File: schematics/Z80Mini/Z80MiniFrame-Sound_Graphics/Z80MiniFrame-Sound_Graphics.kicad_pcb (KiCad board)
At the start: 2 copper layers, 194.3 x 105.4 mm, 65 parts, among them J1 Conn_02x20_Odd_Even, J2 RGB Out, U1 TMS9929A, U12 74LS32, U13 74LS139, U14 TL084, U2 74LS574, U3 74LS574, U4 74LS574, U5 AS6C62256-55PCN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

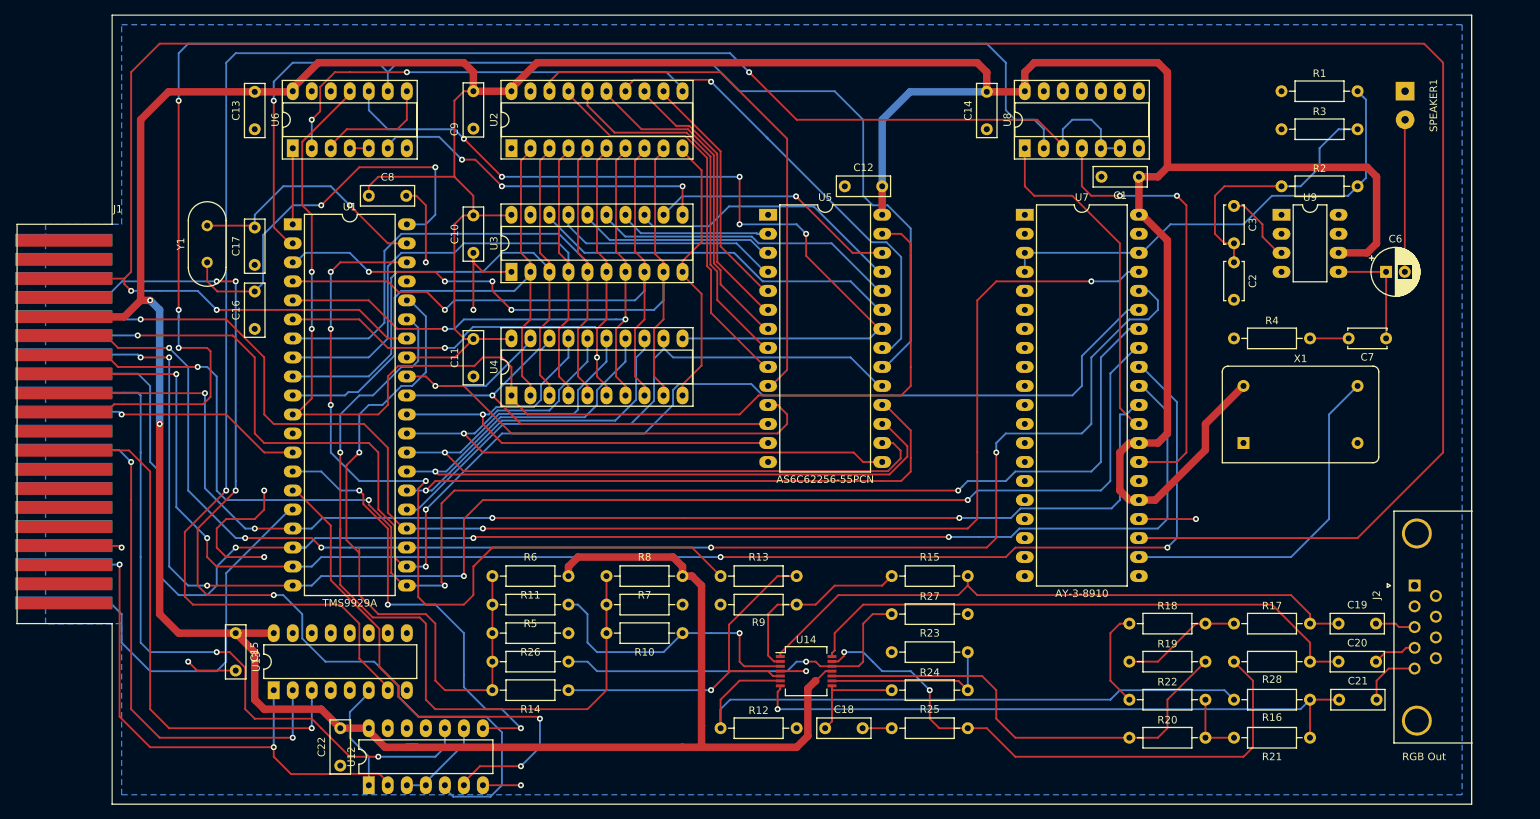
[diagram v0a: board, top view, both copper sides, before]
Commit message: Latest graphics and sound card schematic and PCB modifications
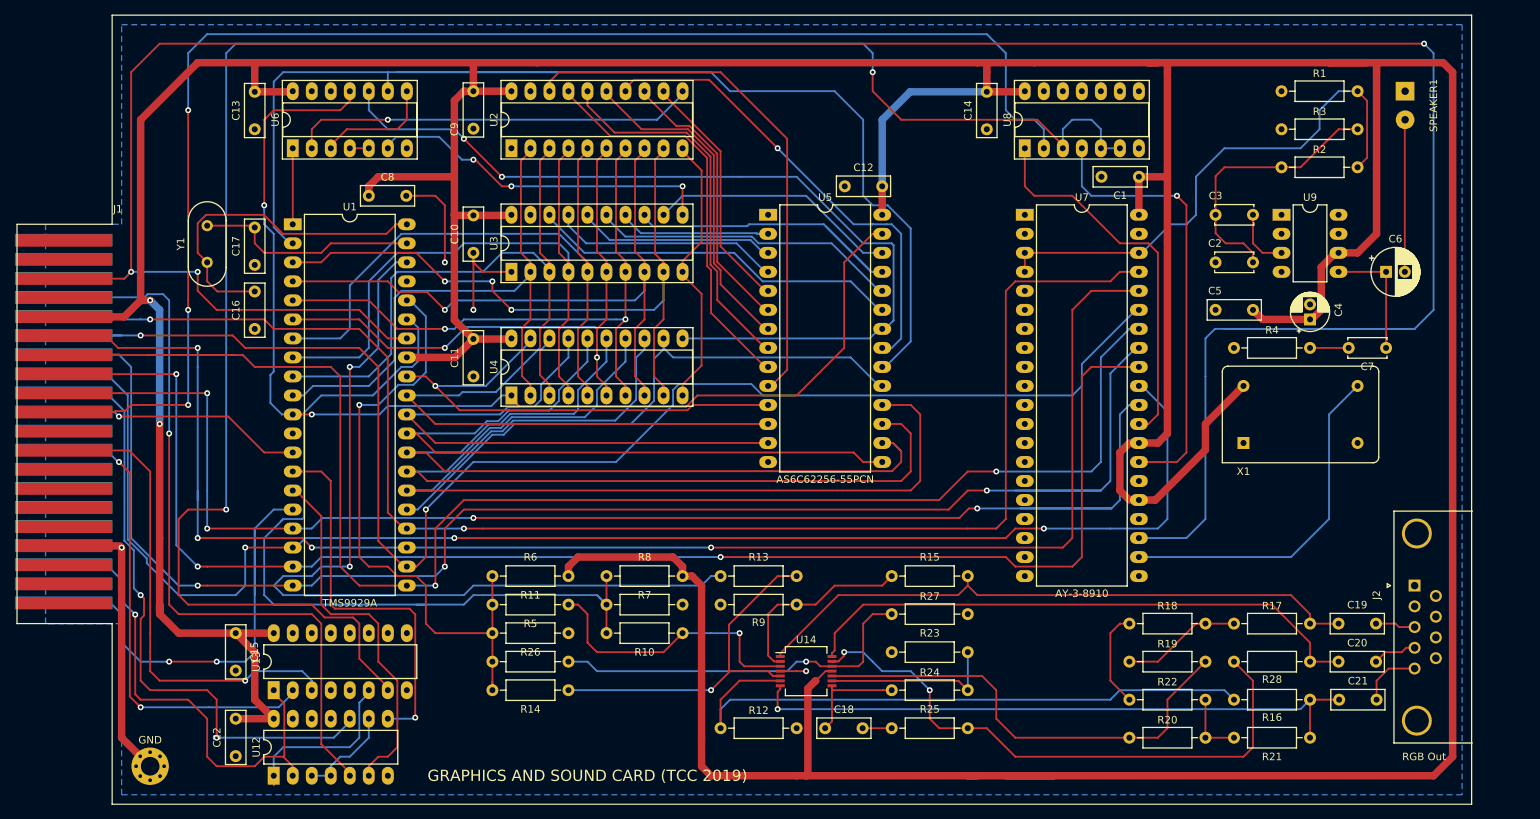
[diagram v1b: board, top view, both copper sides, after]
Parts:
- added C4: 10uF, Capacitor_THT:CP_Radial_D5.0mm_P2.00mm, F.Cu at (218.4, 82.5)
- added C5: 0.1uF, Capacitor_THT:C_Disc_D7.0mm_W2.5mm_P5.00mm, F.Cu at (210.8, 81.3)
- added GND: MountingHole_2.5mm_Pad_Via, MountingHole:MountingHole_2.5mm_Pad_Via, F.Cu at (63.5, 142.2)
- moved C22 14.0 mm to (74.9, 140.9)
- moved U12 12.8 mm to (80.0, 143.5)
- moved C3 2.80 mm to (210.8, 68.6), turned to 180 degrees
- moved R2 2.54 mm to (214.6, 62.2)
- moved C2 2.54 mm to (210.8, 74.9), turned to 180 degrees
- moved C7 1.27 mm to (228.6, 86.4)
- moved R4 1.27 mm to (208.3, 86.4)
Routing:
- net VCC: track 627.4 -> 839.1 mm, vias 2 -> 3
- net Net-(U1-Pad2): track 148.0 -> 188.3 mm, vias 1 -> 0
- net /graphicsProcessor/RD: track 134.3 -> 104.2 mm, vias 4 -> 1
- net /graphicsProcessor/RESET: track 352.9 -> 380.0 mm, vias 2 -> 3
- net Net-(U1-Pad15): track 70.0 -> 49.4 mm, vias 2 -> 0
- net /graphicsProcessor/WR: track 102.4 -> 81.8 mm
- net /D3: track 198.7 -> 215.2 mm, vias 4 -> 2
- net /D7: track 172.1 -> 187.5 mm
- net /A5: track 77.9 -> 63.5 mm
- net /graphicsProcessor/IORQ: track 76.0 -> 64.5 mm, vias 2 -> 1
- net /graphicsProcessor/VD1: track 60.8 -> 72.3 mm, vias 1 -> 0
- net Net-(U1-Pad11): track 166.1 -> 154.9 mm
- net /graphicsProcessor/INT: track 58.2 -> 69.2 mm, vias 0 -> 2
- net Net-(U1-Pad14): track 61.1 -> 51.4 mm, vias 3 -> 1
- net Net-(C16-Pad2): track 54.9 -> 45.3 mm, vias 2 -> 0
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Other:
- net class GND added: clearance 0.2, trace_width 1, via_dia 0.8, via_drill 0.4
- board text added: "GRAPHICS AND SOUND CARD (TCC 2019)"

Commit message: Latest modifications on Graphics-Sound card
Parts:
- added J3: Conn_01x03_Male, Connector_PinHeader_2.00mm:PinHeader_1x03_P2.00mm_Vertical, F.Cu at (208.3, 59.7)
- added JP1: PREAMP_MONO, Connector_PinHeader_2.00mm:PinHeader_2x03_P2.00mm_Vertical, F.Cu at (208.3, 50.8)
- moved R2 10.2 mm to (224.8, 62.2), turned to 180 degrees
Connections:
- R1 pad 2: Net-(R1-Pad2) -> Net-(JP1-Pad1)
- R2 pad 2: Net-(R1-Pad2) -> Net-(JP1-Pad1)
- U7 pad 3: Net-(R1-Pad2) -> Net-(J3-Pad2)
- U7 pad 38: Net-(R1-Pad2) -> Net-(J3-Pad1)
- U7 pad 4: Net-(R1-Pad2) -> Net-(J3-Pad3)
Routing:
- net Net-(R1-Pad2): track 71.6 -> 0.00 mm
- net Net-(J3-Pad3): track 0.00 -> 52.3 mm
- net Net-(J3-Pad2): track 0.00 -> 40.6 mm
- net Net-(JP1-Pad1): track 0.00 -> 34.4 mm
- net Net-(J3-Pad1): track 0.00 -> 26.4 mm
- net Net-(U7-Pad22): track 46.9 -> 40.9 mm
- net Net-(U7-Pad29): track 51.6 -> 48.3 mm
- net /soundGeneration/SND_SEL: track 249.6 -> 251.4 mm

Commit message: Latest modifications
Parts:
- added J4: IO_PORT, Connector_IDC:IDC-Header_2x08_P2.54mm_Vertical, F.Cu at (229.9, 102.9)
- moved R4 16.9 mm to (224.8, 82.5)
- moved C3 14.5 mm to (224.8, 64.8)
- moved C7 14.2 mm to (234.9, 73.7), turned to 270 degrees
- moved C2 12.0 mm to (217.2, 64.8)
- moved C4 10.2 mm to (209.6, 77.5), turned to 270 degrees
- moved C5 7.73 mm to (209.6, 73.7), turned to 90 degrees
- moved J2 3.81 mm to (232.4, 121.9)
- moved X1 3.81 mm to (209.6, 95.2)
- moved R2 2.54 mm to (224.8, 59.7)
- moved R1 1.27 mm to (214.6, 50.8)
- moved R3 1.27 mm to (214.6, 55.9)
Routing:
- net Net-(J4-Pad16): track 0.00 -> 71.2 mm, vias 0 -> 1
- net Net-(J4-Pad3): track 0.00 -> 60.8 mm, vias 0 -> 1
- net Net-(J4-Pad15): track 0.00 -> 55.4 mm, vias 0 -> 1
- net Net-(J4-Pad5): track 0.00 -> 54.0 mm
- net Net-(J4-Pad1): track 0.00 -> 48.8 mm
- net Net-(J4-Pad7): track 0.00 -> 48.6 mm
- net Net-(J4-Pad9): track 0.00 -> 43.5 mm
- net Net-(J4-Pad11): track 0.00 -> 41.6 mm
- net Net-(J4-Pad13): track 0.00 -> 39.3 mm
- net /graphicsProcessor/RESET: track 380.0 -> 348.7 mm, vias 3 -> 4
- net Net-(U7-Pad22): track 40.9 -> 71.7 mm
- net Net-(C2-Pad1): track 36.5 -> 15.0 mm
- net /D7: track 187.5 -> 172.2 mm
- net /D6: track 198.1 -> 213.4 mm, vias 3 -> 4
- net /D4: track 205.8 -> 192.3 mm
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
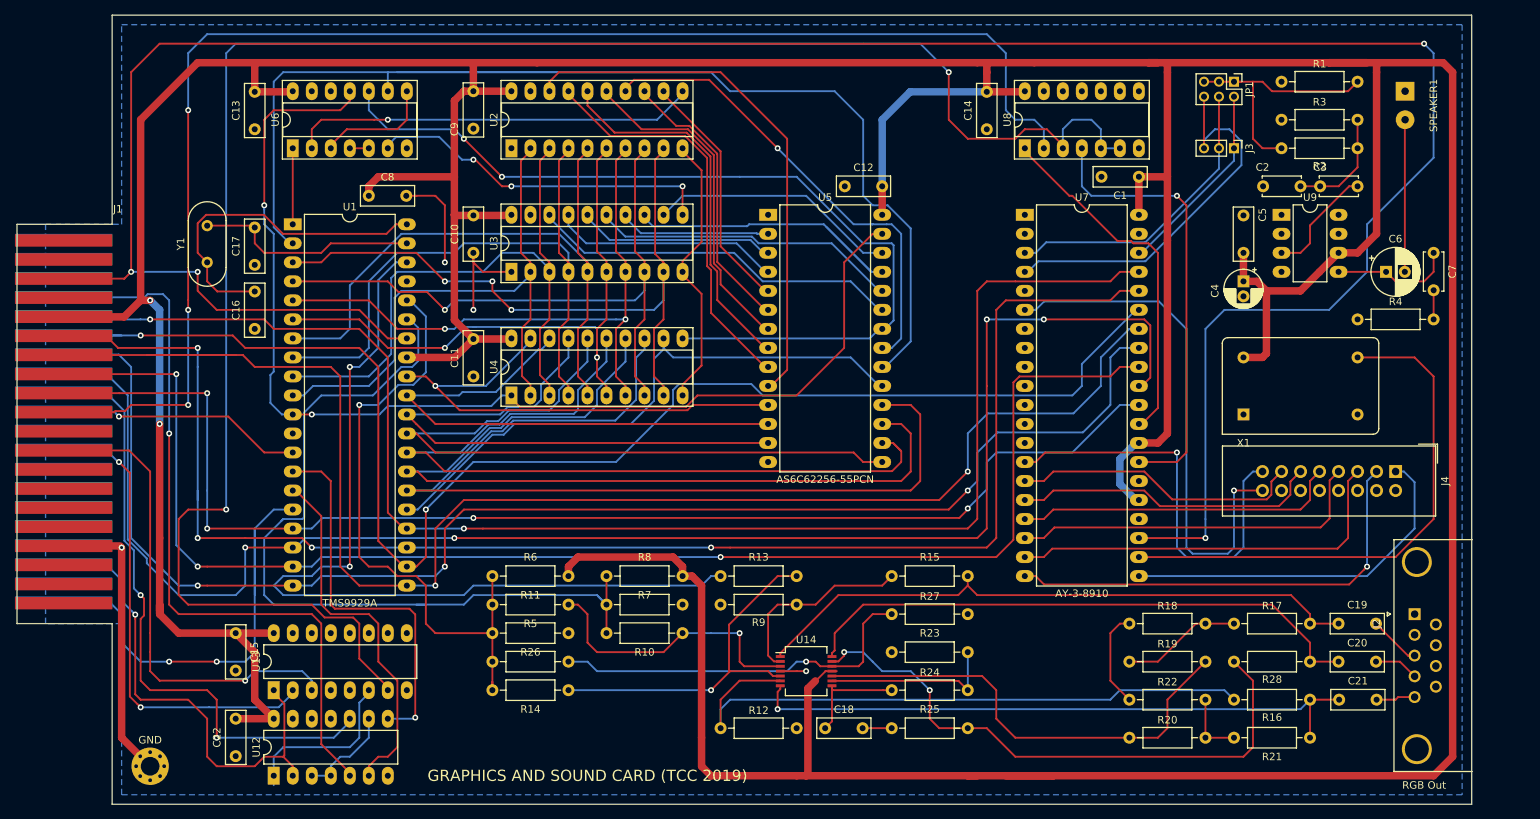
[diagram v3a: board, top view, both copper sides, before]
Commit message: Latest modifications and update to v1.1 and first successifully VDP routines test.
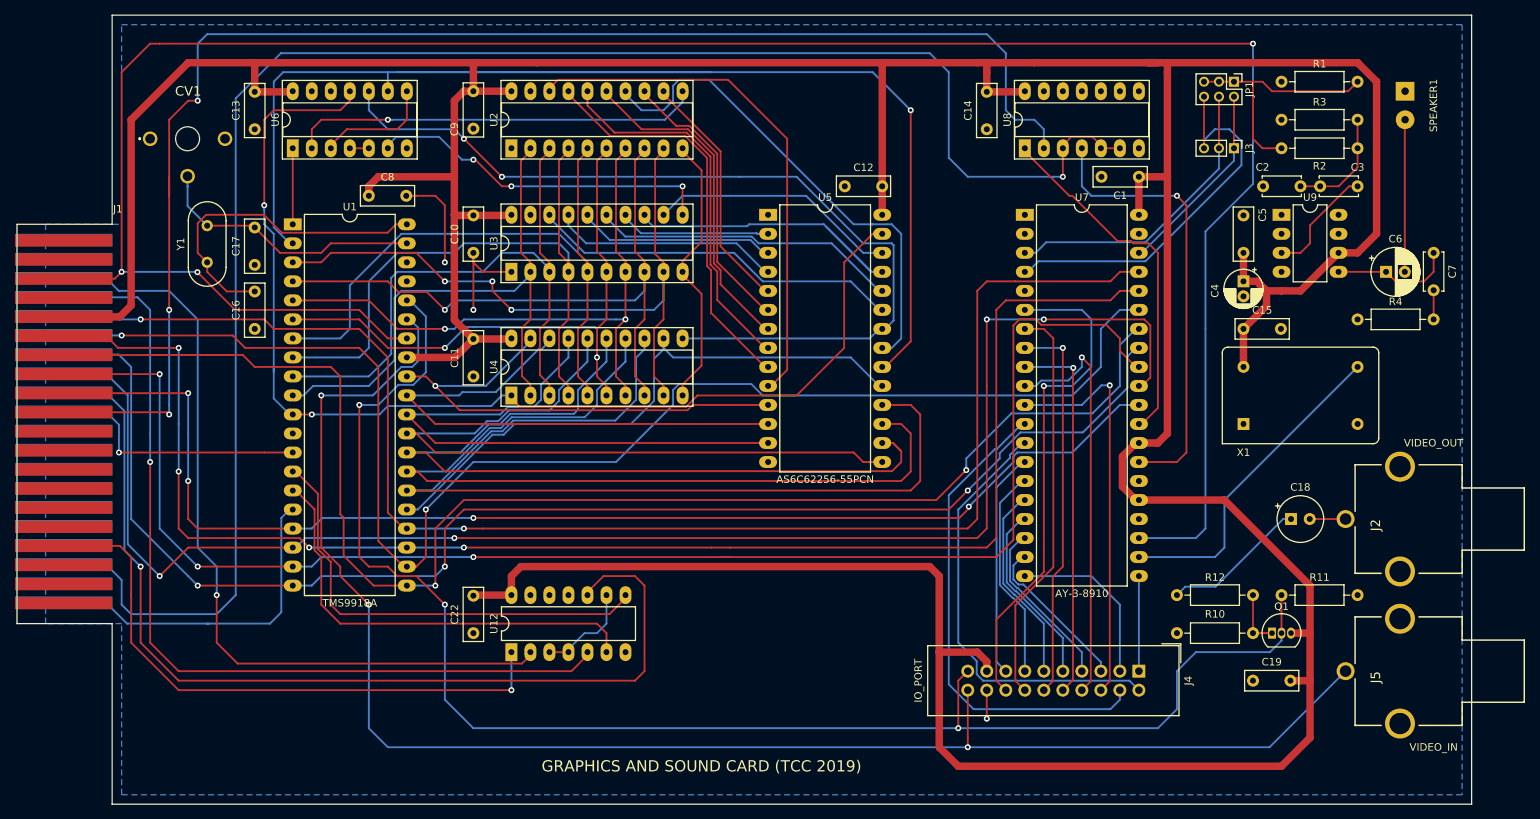
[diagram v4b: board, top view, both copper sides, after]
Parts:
- removed C20, C21: 47pF, Capacitor_THT:C_Disc_D7.0mm_W2.5mm_P5.00mm
- removed GND: MountingHole_2.5mm_Pad_Via, MountingHole:MountingHole_2.5mm_Pad_Via
- removed R13, R14, R15, R16, R17, R19, R20, R21, R23, R24, R25, R26, R9: 100K, Resistor_THT:R_Axial_DIN0207_L6.3mm_D2.5mm_P10.16mm_Horizontal
- removed R18: 47K, Resistor_THT:R_Axial_DIN0207_L6.3mm_D2.5mm_P10.16mm_Horizontal
- removed R22: 12K, Resistor_THT:R_Axial_DIN0207_L6.3mm_D2.5mm_P10.16mm_Horizontal
- removed R27, R28: 170K, Resistor_THT:R_Axial_DIN0207_L6.3mm_D2.5mm_P10.16mm_Horizontal
- removed R5, R7: 1K, Resistor_THT:R_Axial_DIN0207_L6.3mm_D2.5mm_P10.16mm_Horizontal
- removed R6, R8: 2K, Resistor_THT:R_Axial_DIN0207_L6.3mm_D2.5mm_P10.16mm_Horizontal
- removed U13: 74LS139, Package_DIP:DIP-16_W7.62mm_LongPads
- removed U14: TL084, Package_SO:SSOP-14_5.3x6.2mm_P0.65mm
- added CV1: 5-50pF, Capacitor_THT:BFC280831659, F.Cu at (63.5, 58.4)
- added J5: COMP_VIDEOIN, Connector:RCA_Female_902, F.Cu at (238.8, 129.5)
- added Q1: 2N3904, Package_TO_SOT_THT:TO-92_Inline, F.Cu at (213.4, 124.5)
- C16: value 100nF -> 33pf
- C17: value 100nF -> 33pF
- C18: value 47pF -> 220uF; footprint Capacitor_THT:C_Disc_D7.0mm_W2.5mm_P5.00mm -> Capacitor_THT:CP_Radial_Tantal_D6.0mm_P2.50mm
- C19: value 47pF -> 100nF
- J2: value RGB Out -> COMP_VIDEOUT; footprint Connector_Dsub:DSUB-9_Female_Horizontal_P2.77x2.84mm_EdgePinOffset4.94mm_Housed_MountingHolesOffset7.48mm -> Connector:RCA_Female_902
- J4: footprint Connector_IDC:IDC-Header_2x08_P2.54mm_Vertical -> Connector_IDC:IDC-Header_2x10_P2.54mm_Vertical
- R10, R12: value 100K -> 75R
- R11: value 100K -> 470R
- U1: value TMS9929A -> TMS9918A
- Y1: value Crystal -> 10.73MHz
- moved C15 140.6 mm to (209.6, 83.8), turned to 0 degrees
- moved R11 95.3 mm to (214.6, 119.4), turned to 0 degrees
- moved R10 76.2 mm to (210.8, 124.5)
- moved C18 68.2 mm to (215.9, 109.2)
- moved R12 63.5 mm to (200.7, 119.4)
- moved J4 43.4 mm to (195.6, 129.5)
- moved U12 35.8 mm to (111.8, 127.0)
- moved C22 35.7 mm to (106.7, 124.5)
- moved J2 14.2 mm to (238.8, 109.2)
- moved C19 13.7 mm to (210.8, 130.8)
- moved X1 1.27 mm to (209.6, 96.5)
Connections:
- C19 pad 1: /graphicsProcessor/RYBYRGBConverter/RED -> GND
- C19 pad 2: /graphicsProcessor/RYBYRGBConverter/R -> VCC
- J1 pad 23: /A4 -> Net-(J1-Pad23)
- J1 pad 24: /A5 -> Net-(J1-Pad24)
- J1 pad 33: GND -> /graphicsProcessor/VD_SEL
- J1 pad 36: /graphicsProcessor/IORQ -> /soundGeneration/SND_SEL
- J1 pad 6: Net-(J1-Pad6) -> /graphicsProcessor/IORQ
- J2 pad 1: GND -> Net-(C18-Pad2)
- J2 pad 3: /graphicsProcessor/RYBYRGBConverter/R -> (no net)
- R10 pad 1: Net-(R10-Pad1) -> Net-(Q1-Pad1)
- R10 pad 2: /graphicsProcessor/RYBYRGBConverter/R-Y -> GND
- R11 pad 1: Net-(R10-Pad1) -> /graphicsProcessor/COMVID
- R11 pad 2: /graphicsProcessor/RYBYRGBConverter/Y -> GND
- R12 pad 1: Net-(R12-Pad1) -> Net-(C18-Pad1)
- R12 pad 2: GND -> Net-(Q1-Pad1)
- U1 pad 35: /graphicsProcessor/RYBYRGBConverter/R-Y -> /graphicsProcessor/EXTV
- U1 pad 36: /graphicsProcessor/RYBYRGBConverter/Y -> /graphicsProcessor/COMVID
- U1 pad 38: /graphicsProcessor/RYBYRGBConverter/B-Y -> Net-(U1-Pad38)
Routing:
- net /graphicsProcessor/EXTV: track 0.00 -> 211.7 mm, vias 0 -> 3
- net /graphicsProcessor/COMVID: track 0.00 -> 204.1 mm, vias 0 -> 3
- net VCC: track 828.6 -> 662.2 mm, vias 2 -> 0
- net /graphicsProcessor/RYBYRGBConverter/B-Y: track 117.9 -> 0.00 mm, vias 2 -> 0
- net /graphicsProcessor/RYBYRGBConverter/R-Y: track 110.7 -> 0.00 mm
- net Net-(R12-Pad1): track 85.6 -> 0.00 mm
- net /graphicsProcessor/RYBYRGBConverter/BLUE: track 83.9 -> 0.00 mm, vias 1 -> 0
- net /graphicsProcessor/RYBYRGBConverter/Y: track 83.2 -> 0.00 mm, vias 1 -> 0
- net /graphicsProcessor/RYBYRGBConverter/RED: track 82.9 -> 0.00 mm
- net Net-(R25-Pad1): track 78.0 -> 0.00 mm, vias 2 -> 0
- net Net-(C20-Pad1): track 76.8 -> 0.00 mm
- net /A4: track 69.5 -> 0.00 mm, vias 1 -> 0
- net Net-(J4-Pad4): track 0.00 -> 65.4 mm
- net /A5: track 63.5 -> 0.00 mm, vias 2 -> 0
- net Net-(R19-Pad2): track 62.0 -> 0.00 mm
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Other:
- board text added: "VIDEO_IN"
- board text added: "VIDEO_OUT"
